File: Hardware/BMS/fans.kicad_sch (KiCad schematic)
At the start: 33 parts, among them J1301 Conn_02x03_Top_Bottom, Q1301 DMN10H220L, Q1302 DMN10H220L, U1303 MIC28514T-E_PHA

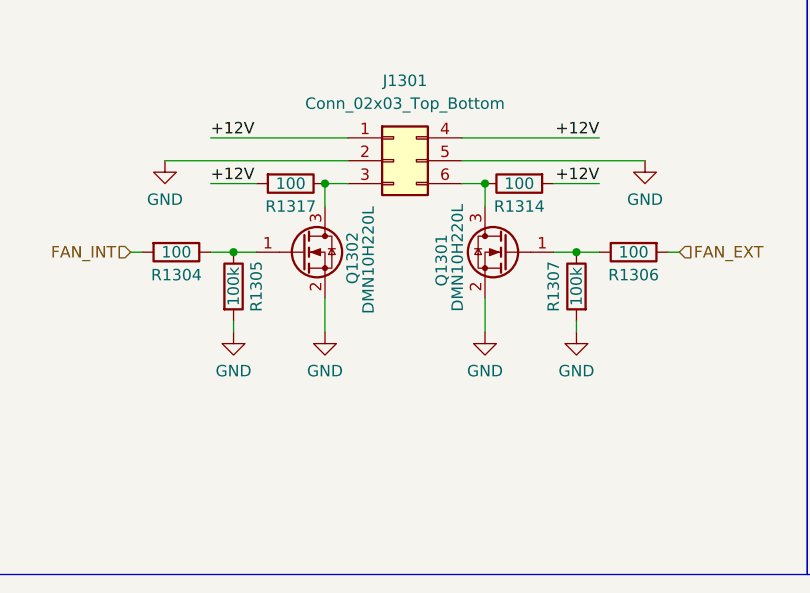
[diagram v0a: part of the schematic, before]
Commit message: fab updates to bms, power board, fet board
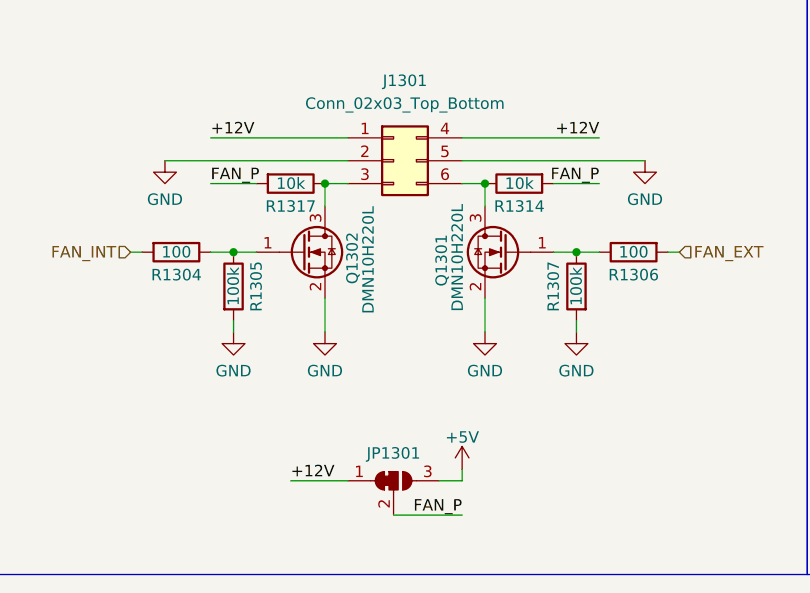
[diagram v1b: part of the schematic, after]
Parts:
- added JP1301: SolderJumper_3_Bridged12, Jumper:SolderJumper-3_P1.3mm_Bridged12_RoundedPad1.0x1.5mm, symbol Jumper:SolderJumper_3_Bridged12
- C1317, C1318, C1319: footprint Capacitor_SMD:C_0603_1608Metric -> Capacitor_SMD:C_0805_2012Metric
- R1314, R1317: value 100 -> 10k
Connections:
- net +12V: now also JP1301.1 (A); no longer R1314.2, R1317.2
- new net +5V: JP1301.3 (B)
- new net FAN_P: JP1301.2 (C), R1314.2, R1317.2
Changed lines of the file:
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@@
 	(wire
 		(pts
+			(xy 67.31 115.57) (xy 73.66 115.57)
+		)
+		(stroke
+			(width 0)
+			(type default)
+		)
+	)
+	(wire
+		(pts
 			(xy 193.04 93.98) (xy 193.04 96.52)
 		)
@@
 	(wire
 		(pts
+			(xy 86.36 115.57) (xy 83.82 115.57)
+		)
+		(stroke
+			(width 0)
+			(type default)
+		)
+	)
+	(wire
+		(pts
 			(xy 185.42 74.93) (xy 185.42 73.66)
 		)
@@
 	(wire
 		(pts
+			(xy 86.36 114.3) (xy 86.36 115.57)
+		)
+		(stroke
+			(width 0)
+			(type default)
+		)
+	)
+	(wire
+		(pts
 			(xy 71.12 85.09) (xy 71.12 82.55)
 		)
@@
 	(wire
 		(pts
+			(xy 78.74 119.38) (xy 86.36 119.38)
+		)
+		(stroke
+			(width 0)
+			(type default)
+		)
+	)
+	(wire
+		(pts
 			(xy 245.11 113.03) (xy 252.73 113.03)
 		)
@@
 		)
 	)
-	(label "+12V"
+	(label "FAN_P"
 		(at 58.42 82.55 0)
 		(effects
@@
 		)
 	)
-	(label "+12V"
+	(label "FAN_P"
 		(at 101.6 82.55 180)
 		(effects
@@
 	)
 	(label "+12V"
+		(at 67.31 115.57 0)
+		(effects
+			(font
+				(size 1.27 1.27)
+			)
+			(justify left bottom)
+		)
+	)
+	(label "FAN_P"
+		(at 86.36 119.38 180)
+		(effects
+			(font
+				(size 1.27 1.27)
+			)
+			(justify right bottom)
+		)
+	)
+	(label "+12V"
 		(at 101.6 77.47 180)
 		(effects
@@
 			)
 		)
-		(property "Value" "100"
+		(property "Value" "10k"
 			(at 67.31 82.55 90)
 			(effects
@@
 			)
 		)
-		(property "Value" "100"
+		(property "Value" "10k"
 			(at 92.71 82.55 90)
 			(effects
@@
 	)
 	(symbol
+		(lib_id "Jumper:SolderJumper_3_Bridged12")
+		(at 78.74 115.57 0)
+		(unit 1)
+		(exclude_from_sim no)
+		(in_bom no)
+		(on_board yes)
+		(dnp no)
+		(property "Reference" "JP1301"
+			(at 78.74 112.522 0)
+			(effects
+				(font
+					(size 1.27 1.27)
+				)
+			)
+		)
+		(property "Value" "SolderJumper_3_Bridged12"
+			(at 78.74 111.76 0)
+			(effects
+				(font
+					(size 1.27 1.27)
+				)
+				(hide yes)
+			)
+		)
+		(property "Footprint" "Jumper:SolderJumper-3_P1.3mm_Bridged12_RoundedPad1.0x1.5mm"
+			(at 78.74 115.57 0)
+			(effects
+				(font
+					(size 1.27 1.27)
+				)
+				(hide yes)
+			)
+		)
+		(property "Datasheet" "~"
+			(at 78.74 115.57 0)
+			(effects
+				(font
+					(size 1.27 1.27)
+				)
+				(hide yes)
+			)
+		)
+		(property "Description" "3-pole Solder Jumper, pins 1+2 closed/bridged"
+			(at 78.74 115.57 0)
+			(effects
+				(font
+					(size 1.27 1.27)
+				)
+				(hide yes)
+			)
+		)
+		(pin "2"
+		)
+		(pin "3"
+		)
+		(pin "1"
+		)
+		(instances
+			(project ""
+				(path "/36848c1b-92a5-46b0-877b-0db2387c679c/499e9990-2ead-48e5-bb1e-d470202346f6"
+					(reference "JP1301")
+					(unit 1)
+				)
+			)
+		)
+	)
+	(symbol
 		(lib_id "OEM:1KR")
 		(at 189.23 96.52 270)
@@
 			)
 		)
-		(property "Footprint" "Capacitor_SMD:C_0603_1608Metric"
+		(property "Footprint" "Capacitor_SMD:C_0805_2012Metric"
 			(at 197.8152 71.12 0)
 			(effects
@@
 			)
 		)
-		(property "Footprint" "Capacitor_SMD:C_0603_1608Metric"
+		(property "Footprint" "Capacitor_SMD:C_0805_2012Metric"
 			(at 220.6752 71.12 0)
 			(effects
@@
 			)
 		)
-		(property "Footprint" "Capacitor_SMD:C_0603_1608Metric"
+		(property "Footprint" "Capacitor_SMD:C_0805_2012Metric"
 			(at 209.2452 71.12 0)
 			(effects
@@
 					(unit 1)
 				)
+			)
+		)
+	)
+	(symbol
+		(lib_name "+5V_1")
+		(lib_id "power:+5V")
+		(at 86.36 114.3 0)
+		(unit 1)
+		(exclude_from_sim no)
+		(in_bom yes)
+		(on_board yes)
+		(dnp no)
+		(property "Reference" "#PWR01312"
+			(at 86.36 118.11 0)
+			(effects
+				(font
+					(size 1.27 1.27)
+				)
+				(hide yes)
+			)
+		)
+		(property "Value" "+5V"
+			(at 86.36 110.744 0)
+			(effects
+				(font
+					(size 1.27 1.27)
+				)
+			)
+		)
+		(property "Footprint" ""
+			(at 86.36 114.3 0)
+			(effects
+				(font
+					(size 1.27 1.27)
+				)
+				(hide yes)
+			)
+		)
+		(property "Datasheet" ""
+			(at 86.36 114.3 0)
+			(effects
+				(font
+					(size 1.27 1.27)
+				)
+				(hide yes)
+			)
+		)
+		(property "Description" "Power symbol creates a global label with name \"+5V\""
+			(at 86.36 114.3 0)
+			(effects
+				(font
+					(size 1.27 1.27)
+				)
+				(hide yes)
+			)
+		)
+		(pin "1"
+		)
+		(instances
+			(project "bms"
+				(path "/36848c1b-92a5-46b0-877b-0db2387c679c/499e9990-2ead-48e5-bb1e-d470202346f6"
+					(reference "#PWR01312")
+					(unit 1)
+				)

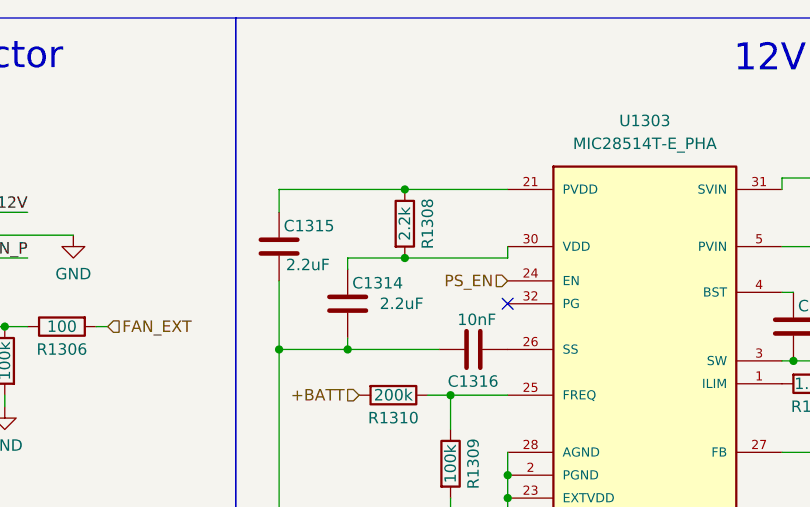
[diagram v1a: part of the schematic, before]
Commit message: basics of CAN and some STM init firmware. Also updated very minor BMS things
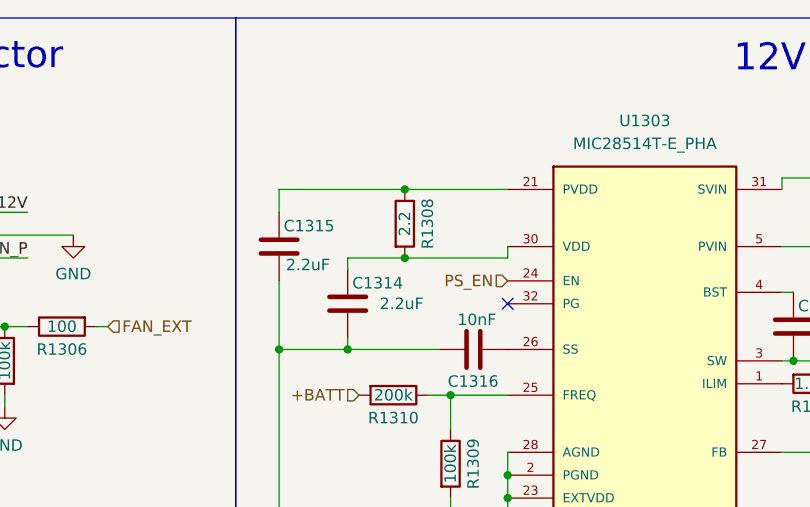
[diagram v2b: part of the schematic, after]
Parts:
- R1308: value 2.2k -> 2.2
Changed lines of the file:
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@@
 			)
 		)
-		(property "Value" "2.2k"
+		(property "Value" "2.2"
 			(at 143.51 78.74 90)
 			(effects
